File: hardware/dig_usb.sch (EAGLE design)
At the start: 182 parts, among them IC101 AT90USB1287-AU, IC102 MAX487CSA, IC103 74HC166D, IC301 LTV-356T, IC302 LTV-356T, IC303 LTV-356T, IC304 LTV-356T, IC305 LTV-356T, IC306 LTV-356T, IC307 LTV-356T, IC308 LTV-356T, IC401 DS1337S, K401 S202S02, K402 S202S02, K403 S202S02, K404 S202S02, K405 S202S02, K406 S202S02, K407 S202S02, K408 S202S02, Q101 16MHz, Q301 BCR191, Q302 BCR191, Q303 BCR191, Q304 BCR191, Q305 BCR191, Q306 BCR191, Q307 BCR191, Q308 BCR191, Q401 32,768kHz, X102 ISP, X301 AKL_230-02, X302 RIA-73-02, X304 RIA-73-02, X305 RIA-73-02, X306 RIA-73-02, X307 RIA-73-02, X308 AKL_230-08, X401 RIA-73-02, X402 RIA-73-02, X403 AKL_230-04, X406 AKL_230-08, X407 RIA-73-02, X408 RIA-73-02, X409 AKL_230-02, X410 RIA-73-02, X411 RIA-73-02, X412 RIA-73-02

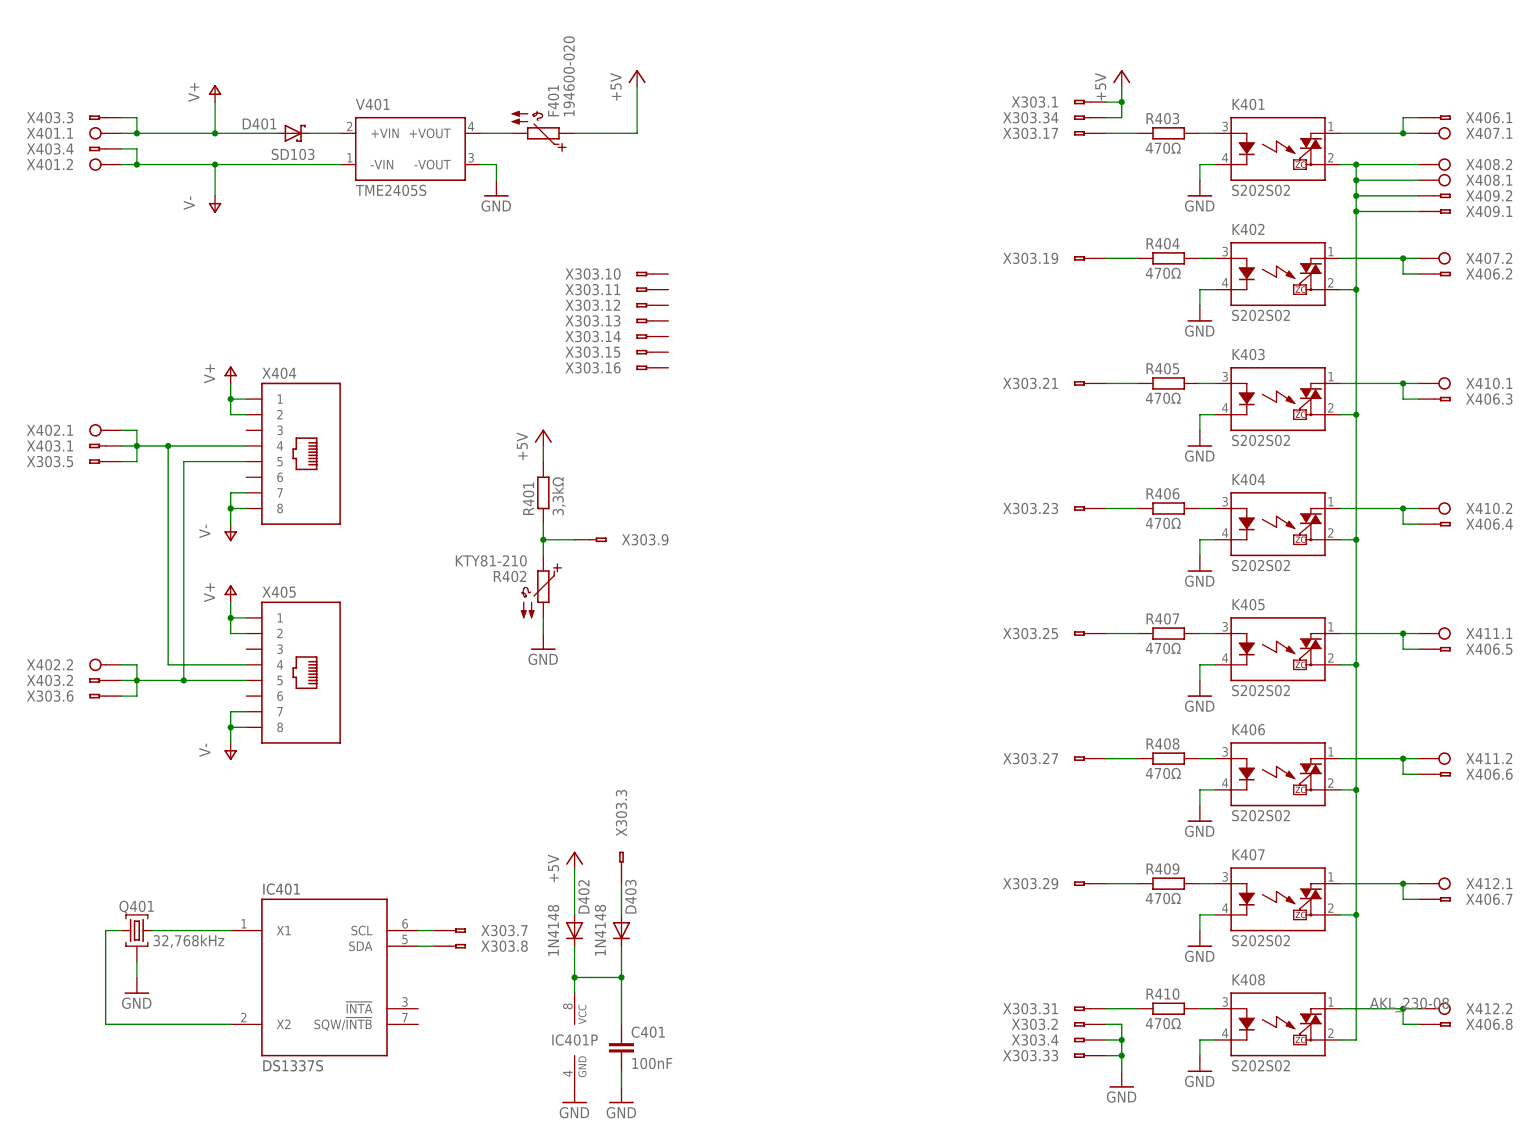
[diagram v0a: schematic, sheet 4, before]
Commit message: Alternativer DC/DC Wandler und Ausgangsfilter hinzugefügt
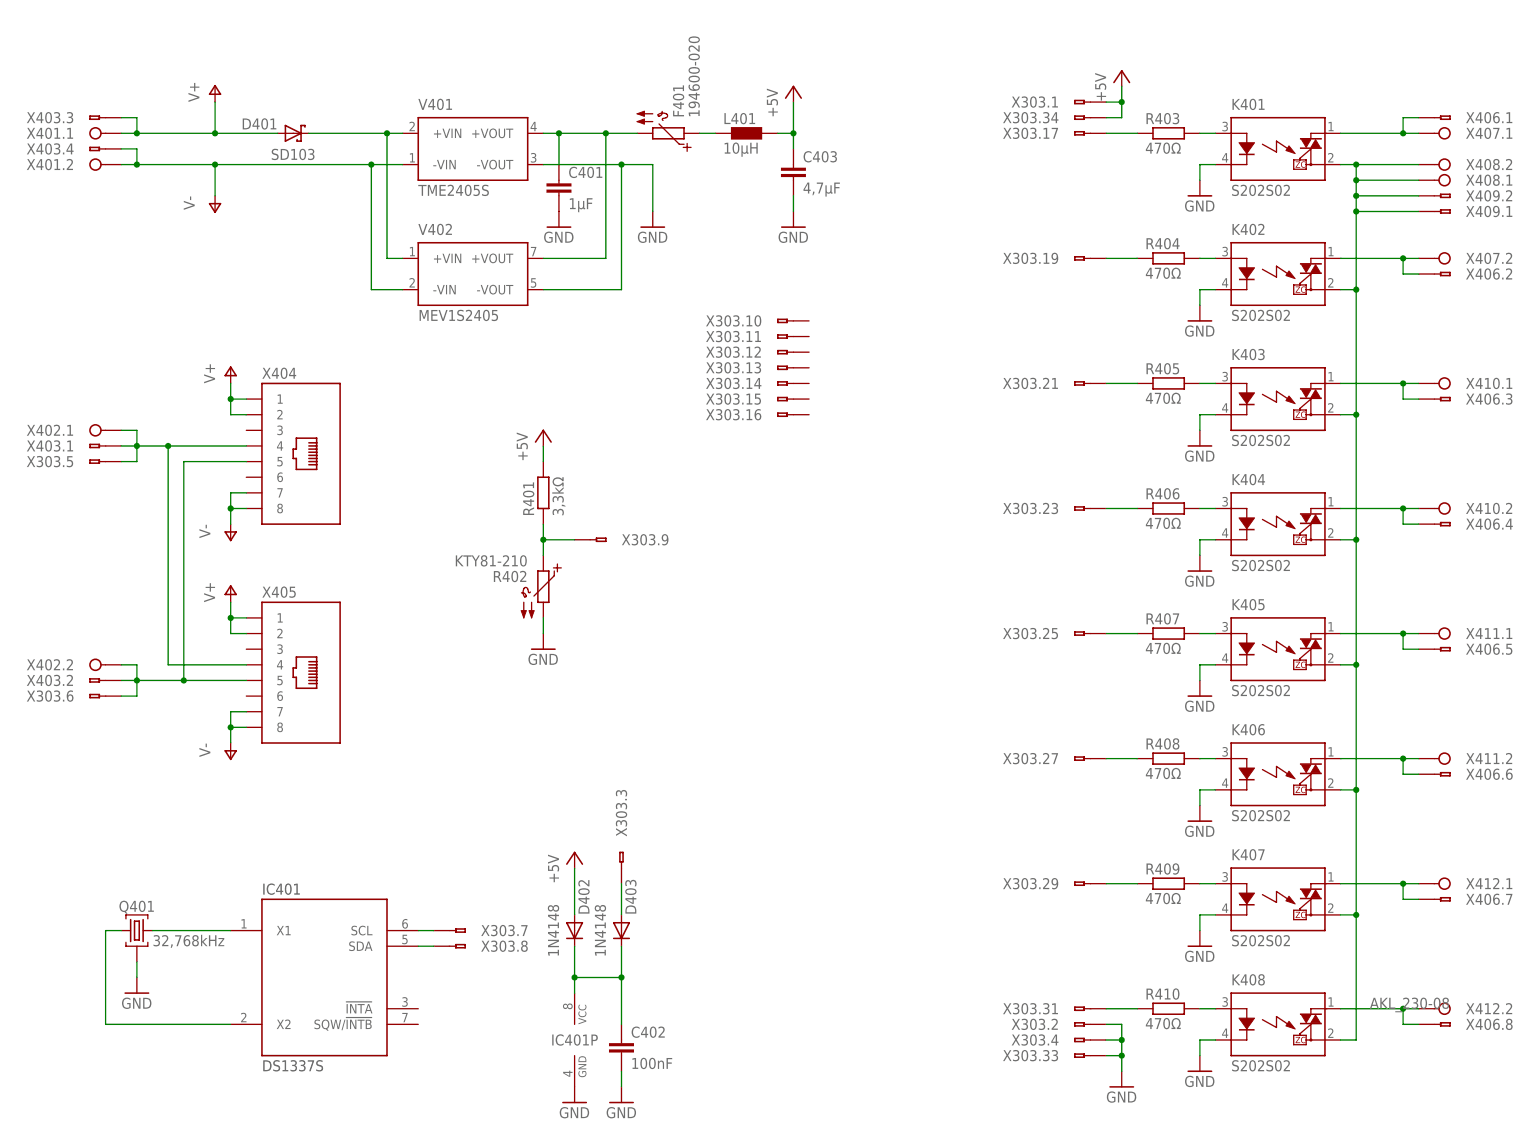
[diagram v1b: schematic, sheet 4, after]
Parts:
- added C402: 100nF, passiv:C_0603
- added C403: 4,7μF, passiv:C_0805
- added L401: 10μH, passiv:L_1812AF
- added V402: MEV1S2405, schaltregler:MEV1S2405
- C401: value 100nF -> 1μF; device passiv:C_0603 -> passiv:C_0805
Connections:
- removed net N$41: F401.2, V401.+VOUT
- new net N$19: C401.1, F401.2, V401.+VOUT, V402.+VOUT
- new net N$24: F401.1, L401.2
- net +5V: now also C403.1, L401.1; no longer F401.1
- net GND: now also C402.2, C403.2, V402.-VOUT
- net N$23: now also V402.+VIN
- net N$64: now also C402.1; no longer C401.1
- net V-: now also V402.-VIN
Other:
- moved on the sheet: C401, F401, V401, X303.10, X303.11, X303.12, X303.13, X303.14, X303.15, X303.16

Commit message: Testpads hinzugefügt
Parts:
- added 0V, 5V, GND, N: (no value), test:TEST_VIA_08
- added ADC0, ADC1, ADC2, ADC3, ADC4, ADC5, ADC6, ADC7: (no value), test:TEST_PAD_SMALL
- added SCL, SDA, SGND: (no value), test:TEST_VIA_06
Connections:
- new net N$148: ADC2.1, X303.11.A
- new net N$149: ADC3.1, X303.12.A
- new net N$150: ADC4.1, X303.13.A
- new net N$151: ADC5.1, X303.14.A
- new net N$152: ADC6.1, X303.15.A
- new net N$153: ADC7.1, X303.16.A
- new net N$41: ADC1.1, X303.10.A
- net +5V: now also 5V.1
- net GND: now also 0V.1, GND.1, SGND.1
- net GNDIO: now also N.1
- net N$131: now also SCL.1
- net N$132: now also SDA.1
- net N$146: now also ADC0.1
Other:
- moved on the sheet: IC401, Q401, X303.10, X303.11, X303.12, X303.13, X303.14, X303.15, X303.16, X303.9
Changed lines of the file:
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@@
 <part name="C403" library="passiv" deviceset="C_" device="0805" value="4,7μF"/>
 <part name="GND407" library="versorgung" deviceset="GND" device=""/>
+<part name="ADC0" library="test" deviceset="TEST" device="_PAD_SMALL"/>
+<part name="ADC1" library="test" deviceset="TEST" device="_PAD_SMALL"/>
+<part name="ADC2" library="test" deviceset="TEST" device="_PAD_SMALL"/>
+<part name="ADC3" library="test" deviceset="TEST" device="_PAD_SMALL"/>
+<part name="ADC4" library="test" deviceset="TEST" device="_PAD_SMALL"/>
+<part name="ADC5" library="test" deviceset="TEST" device="_PAD_SMALL"/>
+<part name="ADC6" library="test" deviceset="TEST" device="_PAD_SMALL"/>
+<part name="ADC7" library="test" deviceset="TEST" device="_PAD_SMALL"/>
+<part name="GND" library="test" deviceset="TEST" device="_VIA_08"/>
+<part name="N" library="test" deviceset="TEST" device="_VIA_08"/>
+<part name="GND1" library="versorgung" deviceset="GND" device=""/>
+<part name="GND2" library="versorgung" deviceset="GNDIO" device=""/>
+<part name="SCL" library="test" deviceset="TEST" device="_VIA_06"/>
+<part name="SDA" library="test" deviceset="TEST" device="_VIA_06"/>
+<part name="SGND" library="test" deviceset="TEST" device="_VIA_06"/>
+<part name="GND3" library="versorgung" deviceset="GND" device=""/>
+<part name="P+1" library="versorgung" deviceset="+5V" device=""/>
+<part name="GND4" library="versorgung" deviceset="GND" device=""/>
+<part name="0V" library="test" deviceset="TEST" device="_VIA_08"/>
+<part name="5V" library="test" deviceset="TEST" device="_VIA_08"/>
 </parts>
 <sheets>
@@
 <instance part="X303" gate=".7" x="91.44" y="43.18" rot="R180"/>
 <instance part="X303" gate=".8" x="91.44" y="40.64" rot="R180"/>
-<instance part="X303" gate=".9" x="114.3" y="106.68" rot="R180"/>
-<instance part="X303" gate=".10" x="142.24" y="142.24"/>
-<instance part="X303" gate=".11" x="142.24" y="139.7"/>
-<instance part="X303" gate=".12" x="142.24" y="137.16"/>
-<instance part="X303" gate=".13" x="142.24" y="134.62"/>
-<instance part="X303" gate=".14" x="142.24" y="132.08"/>
-<instance part="X303" gate=".15" x="142.24" y="129.54"/>
-<instance part="X303" gate=".16" x="142.24" y="127"/>
+<instance part="X303" gate=".9" x="96.52" y="106.68"/>
+<instance part="X303" gate=".10" x="127" y="104.14"/>
+<instance part="X303" gate=".11" x="127" y="101.6"/>
+<instance part="X303" gate=".12" x="127" y="99.06"/>
+<instance part="X303" gate=".13" x="127" y="96.52"/>
+<instance part="X303" gate=".14" x="127" y="93.98"/>
+<instance part="X303" gate=".15" x="127" y="91.44"/>
+<instance part="X303" gate=".16" x="127" y="88.9"/>
 <instance part="X303" gate=".17" x="190.5" y="172.72"/>
 <instance part="X303" gate=".19" x="190.5" y="152.4"/>
@@
 <instance part="X303" gate=".33" x="190.5" y="22.86"/>
 <instance part="X303" gate=".34" x="190.5" y="175.26"/>
-<instance part="IC401" gate="A" x="68.58" y="35.56"/>
-<instance part="Q401" gate="G$1" x="38.1" y="43.18"/>
-<instance part="GND401" gate="1" x="38.1" y="33.02"/>
+<instance part="IC401" gate="A" x="66.04" y="35.56"/>
+<instance part="Q401" gate="G$1" x="35.56" y="43.18"/>
+<instance part="GND401" gate="1" x="35.56" y="33.02"/>
 <instance part="D402" gate="A" x="109.22" y="43.18" rot="R270"/>
 <instance part="D403" gate="A" x="116.84" y="43.18" rot="R270"/>
@@
 <instance part="C403" gate="G$1" x="144.78" y="167.64"/>
 <instance part="GND407" gate="1" x="144.78" y="157.48"/>
+<instance part="ADC0" gate="G$1" x="109.22" y="106.68"/>
+<instance part="ADC1" gate="G$1" x="137.16" y="104.14"/>
+<instance part="ADC2" gate="G$1" x="137.16" y="101.6"/>
+<instance part="ADC3" gate="G$1" x="137.16" y="99.06"/>
+<instance part="ADC4" gate="G$1" x="137.16" y="96.52"/>
+<instance part="ADC5" gate="G$1" x="137.16" y="93.98"/>
+<instance part="ADC6" gate="G$1" x="137.16" y="91.44"/>
+<instance part="ADC7" gate="G$1" x="137.16" y="88.9"/>
+<instance part="GND" gate="G$1" x="137.16" y="71.12" rot="R90"/>
+<instance part="N" gate="G$1" x="144.78" y="71.12" rot="R90"/>
+<instance part="GND1" gate="1" x="137.16" y="63.5"/>
+<instance part="GND2" gate="G$1" x="144.78" y="63.5"/>
+<instance part="SCL" gate="G$1" x="83.82" y="48.26" rot="R90"/>
+<instance part="SDA" gate="G$1" x="83.82" y="35.56" rot="R270"/>
+<instance part="SGND" gate="G$1" x="88.9" y="22.86" rot="R90"/>
+<instance part="GND3" gate="1" x="88.9" y="15.24"/>
+<instance part="P+1" gate="1" x="137.16" y="58.42"/>
+<instance part="GND4" gate="1" x="137.16" y="27.94"/>
+<instance part="0V" gate="G$1" x="137.16" y="33.02" rot="R90"/>
+<instance part="5V" gate="G$1" x="137.16" y="53.34" rot="R270"/>
 </instances>
 <busses>
@@
 <pinref part="Q401" gate="G$1" pin="G"/>
 <pinref part="GND401" gate="1" pin="GND"/>
-<wire x1="38.1" y1="38.1" x2="38.1" y2="35.56" width="0.1524" layer="91"/>
+<wire x1="35.56" y1="38.1" x2="35.56" y2="35.56" width="0.1524" layer="91"/>
 </segment>
 <segment>
@@
 <wire x1="144.78" y1="160.02" x2="144.78" y2="162.56" width="0.1524" layer="91"/>
 </segment>
+<segment>
+<pinref part="GND1" gate="1" pin="GND"/>
+<pinref part="GND" gate="G$1" pin="1"/>
+<wire x1="137.16" y1="68.58" x2="137.16" y2="66.04" width="0.1524" layer="91"/>
+</segment>
+<segment>
+<pinref part="GND3" gate="1" pin="GND"/>
+<pinref part="SGND" gate="G$1" pin="1"/>
+<wire x1="88.9" y1="20.32" x2="88.9" y2="17.78" width="0.1524" layer="91"/>
+</segment>
+<segment>
+<pinref part="GND4" gate="1" pin="GND"/>
+<pinref part="0V" gate="G$1" pin="1"/>
+</segment>
 </net>
 <net name="N$68" class="1">
@@
 <junction x="144.78" y="172.72"/>
 </segment>
+<segment>
+<pinref part="P+1" gate="1" pin="+5V"/>
+<pinref part="5V" gate="G$1" pin="1"/>
+</segment>
 </net>
 <net name="N$16" class="0">
@@
 <pinref part="IC401" gate="A" pin="X1"/>
 <pinref part="Q401" gate="G$1" pin="2"/>
-<wire x1="53.34" y1="43.18" x2="40.64" y2="43.18" width="0.1524" layer="91"/>
+<wire x1="50.8" y1="43.18" x2="38.1" y2="43.18" width="0.1524" layer="91"/>
 </segment>
 </net>
@@
 <pinref part="IC401" gate="A" pin="X2"/>
 <pinref part="Q401" gate="G$1" pin="1"/>
-<wire x1="35.56" y1="43.18" x2="33.02" y2="43.18" width="0.1524" layer="91"/>
-<wire x1="33.02" y1="43.18" x2="33.02" y2="27.94" width="0.1524" layer="91"/>
-<wire x1="33.02" y1="27.94" x2="53.34" y2="27.94" width="0.1524" layer="91"/>
+<wire x1="33.02" y1="43.18" x2="30.48" y2="43.18" width="0.1524" layer="91"/>
+<wire x1="30.48" y1="43.18" x2="30.48" y2="27.94" width="0.1524" layer="91"/>
+<wire x1="30.48" y1="27.94" x2="50.8" y2="27.94" width="0.1524" layer="91"/>
 </segment>
 </net>
@@
 <pinref part="X303" gate=".7" pin="A"/>
 <wire x1="86.36" y1="43.18" x2="83.82" y2="43.18" width="0.1524" layer="91"/>
+<pinref part="SCL" gate="G$1" pin="1"/>
+<wire x1="83.82" y1="43.18" x2="81.28" y2="43.18" width="0.1524" layer="91"/>
+<wire x1="83.82" y1="45.72" x2="83.82" y2="43.18" width="0.1524" layer="91"/>
+<junction x="83.82" y="43.18"/>
 </segment>
 </net>
@@
 <pinref part="X303" gate=".8" pin="A"/>
 <wire x1="86.36" y1="40.64" x2="83.82" y2="40.64" width="0.1524" layer="91"/>
+<pinref part="SDA" gate="G$1" pin="1"/>
+<wire x1="83.82" y1="40.64" x2="81.28" y2="40.64" width="0.1524" layer="91"/>
+<wire x1="83.82" y1="40.64" x2="83.82" y2="38.1" width="0.1524" layer="91"/>
+<junction x="83.82" y="40.64"/>
 </segment>
 </net>
@@
 <pinref part="X303" gate=".9" pin="A"/>
 <wire x1="104.14" y1="106.68" x2="104.14" y2="109.22" width="0.1524" layer="91"/>
-<wire x1="109.22" y1="106.68" x2="104.14" y2="106.68" width="0.1524" layer="91"/>
+<wire x1="101.6" y1="106.68" x2="104.14" y2="106.68" width="0.1524" layer="91"/>
 <junction x="104.14" y="106.68"/>
+<pinref part="ADC0" gate="G$1" pin="1"/>
+<wire x1="104.14" y1="106.68" x2="106.68" y2="106.68" width="0.1524" layer="91"/>
 </segment>
 </net>
@@
 </segment>
 </net>
+<net name="N$41" class="0">
+<segment>
+<pinref part="X303" gate=".10" pin="A"/>
+<pinref part="ADC1" gate="G$1" pin="1"/>
+<wire x1="134.62" y1="104.14" x2="132.08" y2="104.14" width="0.1524" layer="91"/>
+</segment>
+</net>
+<net name="N$148" class="0">
+<segment>
+<pinref part="X303" gate=".11" pin="A"/>
+<pinref part="ADC2" gate="G$1" pin="1"/>
+<wire x1="134.62" y1="101.6" x2="132.08" y2="101.6" width="0.1524" layer="91"/>
+</segment>
+</net>
+<net name="N$149" class="0">
+<segment>
+<pinref part="X303" gate=".12" pin="A"/>
+<pinref part="ADC3" gate="G$1" pin="1"/>
+<wire x1="134.62" y1="99.06" x2="132.08" y2="99.06" width="0.1524" layer="91"/>
+</segment>
+</net>
+<net name="N$150" class="0">
+<segment>
+<pinref part="X303" gate=".13" pin="A"/>
+<pinref part="ADC4" gate="G$1" pin="1"/>
+<wire x1="134.62" y1="96.52" x2="132.08" y2="96.52" width="0.1524" layer="91"/>
+</segment>
+</net>
+<net name="N$151" class="0">
+<segment>
+<pinref part="X303" gate=".14" pin="A"/>
+<pinref part="ADC5" gate="G$1" pin="1"/>
+<wire x1="134.62" y1="93.98" x2="132.08" y2="93.98" width="0.1524" layer="91"/>
+</segment>
+</net>
+<net name="N$152" class="0">
+<segment>
+<pinref part="X303" gate=".15" pin="A"/>
+<pinref part="ADC6" gate="G$1" pin="1"/>
+<wire x1="134.62" y1="91.44" x2="132.08" y2="91.44" width="0.1524" layer="91"/>
+</segment>
+</net>
+<net name="N$153" class="0">
+<segment>
+<pinref part="X303" gate=".16" pin="A"/>
+<pinref part="ADC7" gate="G$1" pin="1"/>
+<wire x1="134.62" y1="88.9" x2="132.08" y2="88.9" width="0.1524" layer="91"/>
+</segment>
+</net>
+<net name="GNDIO" class="1">
+<segment>
+<pinref part="N" gate="G$1" pin="1"/>
+<pinref part="GND2" gate="G$1" pin="GNDIO"/>
+<wire x1="144.78" y1="68.58" x2="144.78" y2="66.04" width="0.1524" layer="91"/>
+</segment>
+</net>
